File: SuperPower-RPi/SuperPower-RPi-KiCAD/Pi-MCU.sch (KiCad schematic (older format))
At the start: 39 parts, among them J10 Conn_01x04, J11 QWIIC_Connector, J12 DNP, J5 Conn_01x06, J7 Conn_01x03, J8 Conn_02x05_Odd_Even, J9 Conn_01x02, SW1 Tact, U3 STM32F412RETx, U4 ATtiny85-20SU, U5 ME6210A33M3G

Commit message: Chose component for Zener Diode and imported into PCB.
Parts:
- removed D6: D_Small, Diode_SMD:D_SOD-523, symbol Device:D_Small
- added D6: BZT585B13T-7, Diode_SMD:D_SOD-523, symbol Device:D_Zener_Small
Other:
- note added: "DotStar indicator"
- note added: "Extra I2C buss conn."
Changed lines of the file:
@@
-$EndComp
-$Comp
-L Device:D_Small D6
-U 1 1 5FAB9400
-P 6200 9650
-F 0 "D6" V 6246 9580 50  0000 R CNN
-F 1 "D_Small" V 6155 9580 50  0000 R CNN
-F 2 "Diode_SMD:D_SOD-523" V 6200 9650 50  0001 C CNN
-F 3 "~" V 6200 9650 50  0001 C CNN
-F 4 "FIX FOOTPRINT" H 6200 9650 50  0001 C CNN "Mfg"
-	1    6200 9650
-	0    -1   -1   0
 $EndComp
 $Comp
@@
 	1    0    0    -1
 $EndComp
+$Comp
+L Device:D_Zener_Small D?
+U 1 1 5FCDC76C
+P 6200 9650
+AR Path="/5F6AC66E/5FCDC76C" Ref="D?"  Part="1"
+AR Path="/5F6AC872/5FCDC76C" Ref="D6"  Part="1"
+F 0 "D6" V 6154 9720 50  0000 L CNN
+F 1 "BZT585B13T-7" V 6245 9720 50  0000 L CNN
+F 2 "Diode_SMD:D_SOD-523" V 6200 9650 50  0001 C CNN
+F 3 "https://www.diodes.com/assets/Datasheets/BZT585BxVxT.pdf" V 6200 9650 50  0001 C CNN
+F 4 "Diodes Incorporated" H 6200 9650 50  0001 C CNN "Mfg"
+F 5 "BZT585B13T-7" H 6200 9650 50  0001 C CNN "Mfg PN"
+F 6 "BZT585B13T-7DICT-ND" H 6200 9650 50  0001 C CNN "Digi-Key PN"
+	1    6200 9650
+	0    -1   -1   0
+$EndComp
+Text Notes 3500 10800 0    50   ~ 0
+Extra I2C buss conn.
+Text Notes 7950 10850 0    50   ~ 0
+DotStar indicator
 $EndSCHEMATC

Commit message: Updated meta-data.
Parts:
- C25, D8, JP1, JP4, JP5, JP6, R15, R25, R26, R27: Mfg (none) -> DNP
- C30: footprint Capacitor_SMD:C_0603_1608Metric -> Capacitor_SMD:C_0402_1005Metric
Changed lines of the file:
@@
 Text Label 2200 9600 2    50   ~ 0
 UART_TX
+Text Notes 3500 10800 0    50   ~ 0
+Extra I2C buss conn.
+Text Notes 7950 10850 0    50   ~ 0
+DotStar indicator
 $Comp
 L Device:R_Small R14
@@
 F 2 "Capacitor_SMD:C_0603_1608Metric" H 12000 5650 50  0001 C CNN
 F 3 "~" H 12000 5650 50  0001 C CNN
+F 4 "DNP" H 12000 5650 50  0001 C CNN "Mfg"
 	1    12000 5650
 	0    -1   1    0
@@
 F 0 "C30" H 5308 5104 50  0000 R CNN
 F 1 "10nF" H 5308 5195 50  0000 R CNN
-F 2 "Capacitor_SMD:C_0603_1608Metric" H 5400 5150 50  0001 C CNN
+F 2 "Capacitor_SMD:C_0402_1005Metric" H 5400 5150 50  0001 C CNN
 F 3 "~" H 5400 5150 50  0001 C CNN
 	1    5400 5150
@@
 F 2 "Resistor_SMD:R_0603_1608Metric" H 3250 10100 50  0001 C CNN
 F 3 "~" H 3250 10100 50  0001 C CNN
+F 4 "DNP" H 3250 10100 50  0001 C CNN "Mfg"
 	1    3250 10100
 	1    0    0    -1
@@
 F 2 "Resistor_SMD:R_0603_1608Metric" H 3550 10100 50  0001 C CNN
 F 3 "~" H 3550 10100 50  0001 C CNN
+F 4 "DNP" H 3550 10100 50  0001 C CNN "Mfg"
 	1    3550 10100
 	1    0    0    -1
@@
 F 2 "Jumper:SolderJumper-2_P1.3mm_Bridged_Pad1.0x1.5mm" H 5200 5800 50  0001 C CNN
 F 3 "~" H 5200 5800 50  0001 C CNN
+F 4 "DNP" H 5200 5800 50  0001 C CNN "Mfg"
 	1    5200 5800
 	1    0    0    -1
@@
 F 2 "LED_SMD:LED_0603_1608Metric" H 14650 6400 50  0001 C CNN
 F 3 "~" H 14650 6400 50  0001 C CNN
+F 4 "DNP" H 14650 6400 50  0001 C CNN "Mfg"
 	1    14650 6400
 	0    -1   -1   0
@@
 F 2 "Resistor_SMD:R_0603_1608Metric" H 14650 6100 50  0001 C CNN
 F 3 "~" H 14650 6100 50  0001 C CNN
+F 4 "DNP" H 14650 6100 50  0001 C CNN "Mfg"
 	1    14650 6100
 	1    0    0    1
@@
 F 2 "Resistor_SMD:R_0603_1608Metric" H 13150 6500 50  0001 C CNN
 F 3 "~" H 13150 6500 50  0001 C CNN
+F 4 "DNP" H 13150 6500 50  0001 C CNN "Mfg"
 	1    13150 6500
 	1    0    0    -1
@@
 F 2 "SuperPower-RPi-KiCAD:PinHeader_1x02_P2.54mm_Vertical_Shorted" H 3450 4250 50  0001 C CNN
 F 3 "~" H 3450 4250 50  0001 C CNN
+F 4 "DNP" H 3450 4250 50  0001 C CNN "Mfg"
 	1    3450 4250
 	1    0    0    -1
@@
 F 2 "Jumper:SolderJumper-2_P1.3mm_Open_Pad1.0x1.5mm" H 2500 5900 50  0001 C CNN
 F 3 "~" H 2500 5900 50  0001 C CNN
+F 4 "DNP" H 2500 5900 50  0001 C CNN "Mfg"
 	1    2500 5900
 	1    0    0    -1
@@
 F 2 "Jumper:SolderJumper-2_P1.3mm_Open_Pad1.0x1.5mm" H 9650 900 50  0001 C CNN
 F 3 "~" H 9650 900 50  0001 C CNN
+F 4 "DNP" H 9650 900 50  0001 C CNN "Mfg"
 	1    9650 900
 	1    0    0    -1
@@
 	0    -1   -1   0
 $EndComp
-Text Notes 3500 10800 0    50   ~ 0
-Extra I2C buss conn.
-Text Notes 7950 10850 0    50   ~ 0
-DotStar indicator
 $EndSCHEMATC

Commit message: Updated 1uF caps to 0402 package.
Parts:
- C32: footprint Capacitor_SMD:C_0603_1608Metric -> Capacitor_SMD:C_0402_1005Metric; Digi-Key PN (none) -> 490-10017-1-ND; Mfg (none) -> Murata Electronics; Mfg PN (none) -> GRM155R61E105KA12D
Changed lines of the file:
@@
 F 0 "C32" H 5708 5104 50  0000 R CNN
 F 1 "1.0uF" H 5708 5195 50  0000 R CNN
-F 2 "Capacitor_SMD:C_0603_1608Metric" H 5800 5150 50  0001 C CNN
+F 2 "Capacitor_SMD:C_0402_1005Metric" H 5800 5150 50  0001 C CNN
 F 3 "~" H 5800 5150 50  0001 C CNN
+F 4 "490-10017-1-ND" H 5800 5150 50  0001 C CNN "Digi-Key PN"
+F 5 "Murata Electronics" H 5800 5150 50  0001 C CNN "Mfg"
+F 6 "GRM155R61E105KA12D" H 5800 5150 50  0001 C CNN "Mfg PN"
 	1    5800 5150
 	-1   0    0    -1

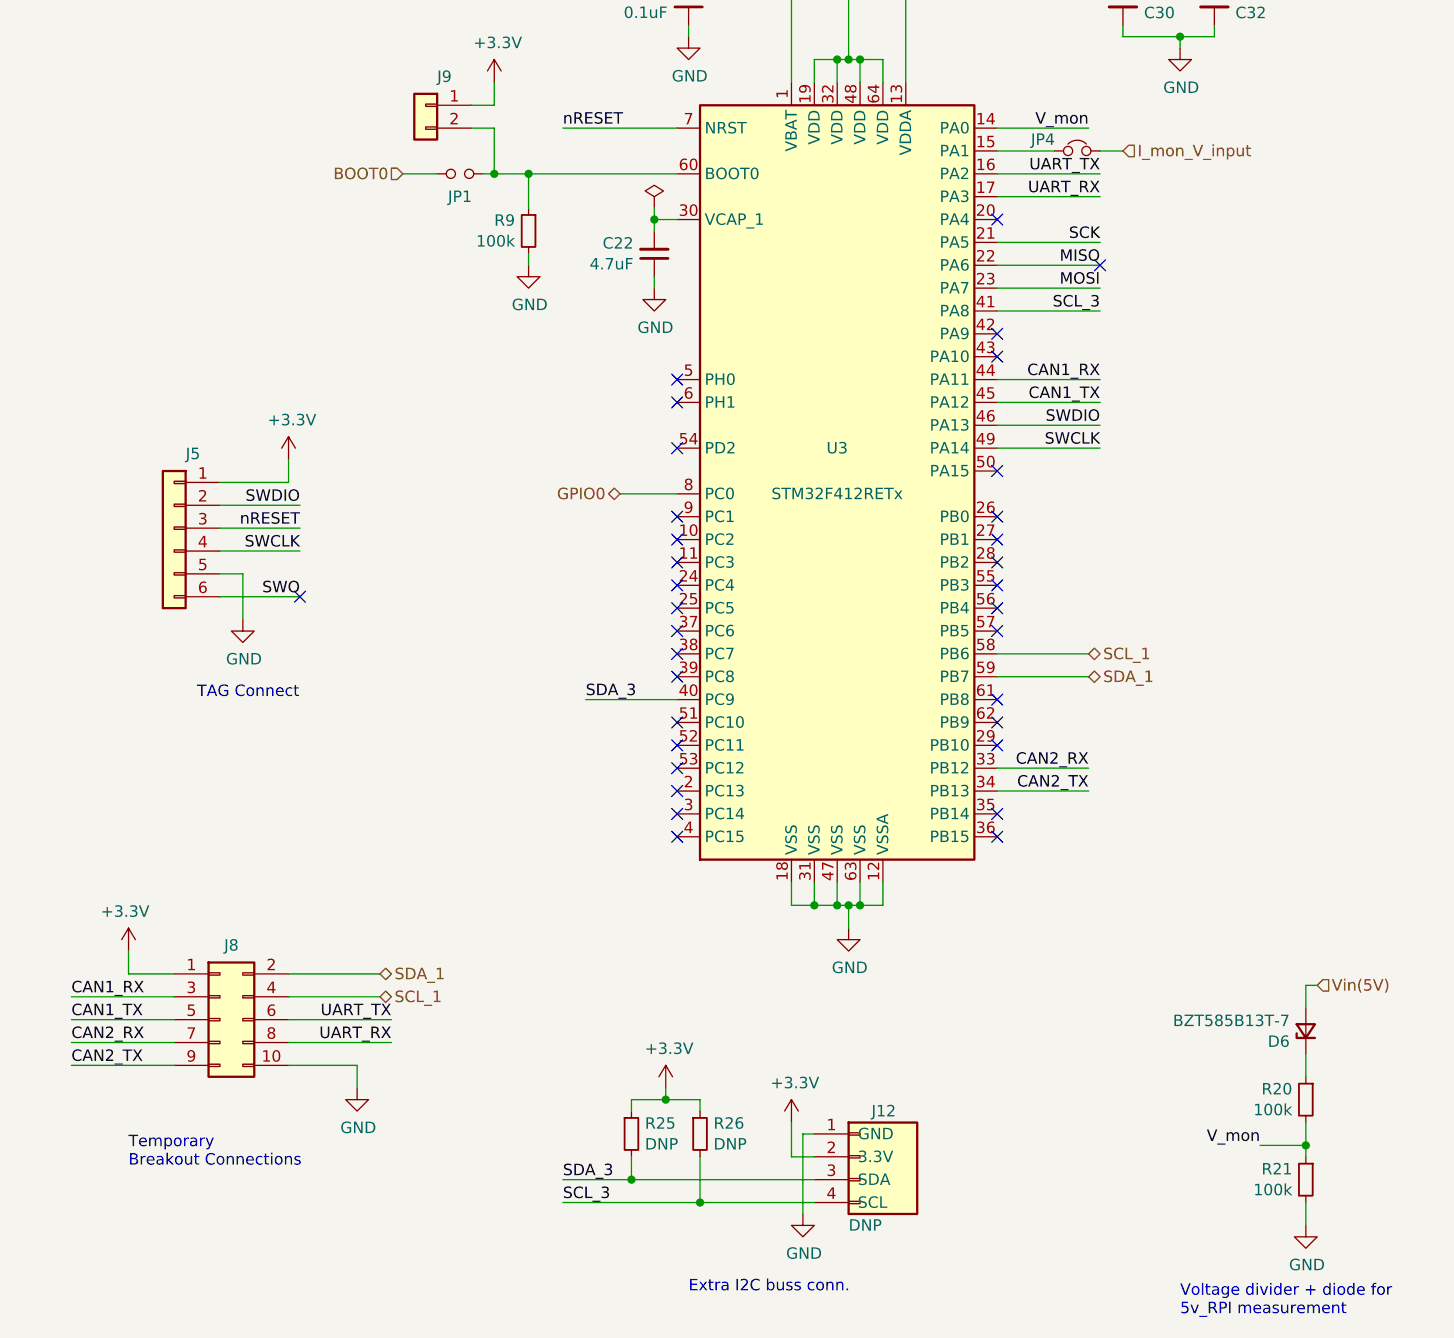
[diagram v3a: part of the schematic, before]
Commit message: Added Jumper to PC13 for bootloader switch.
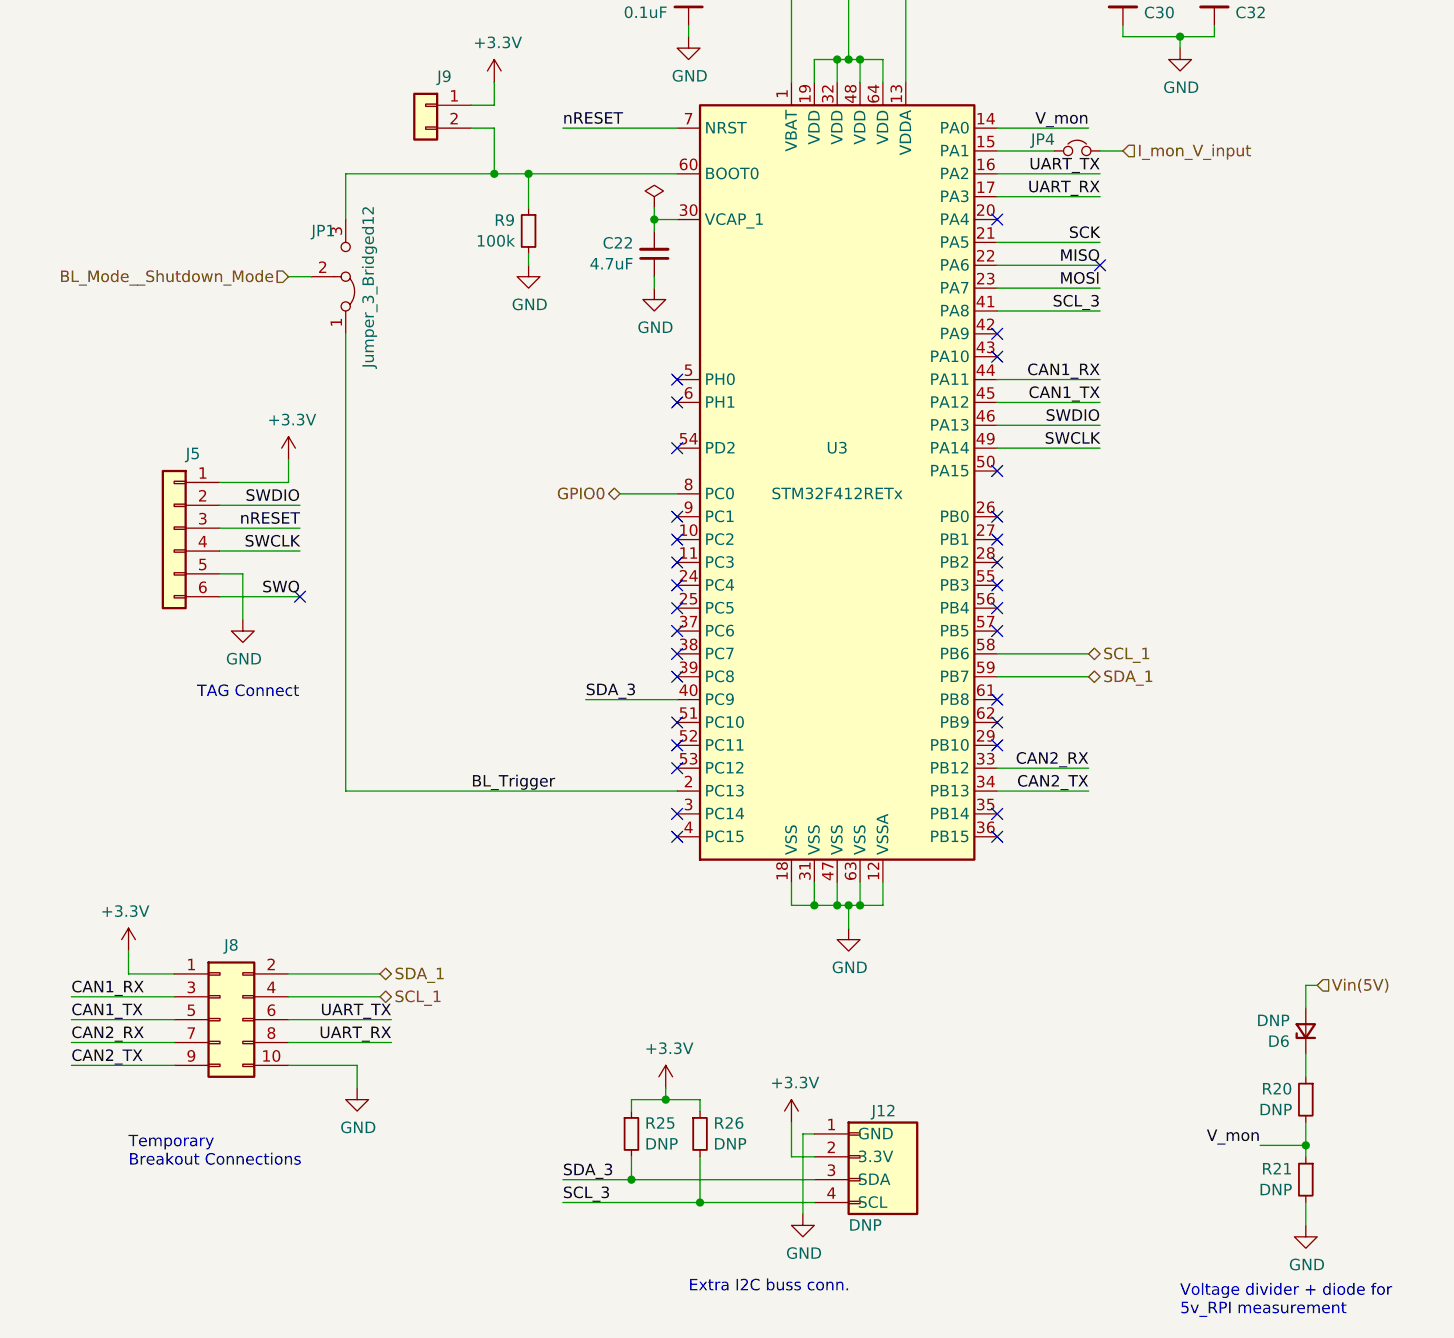
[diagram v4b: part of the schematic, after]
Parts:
- removed JP1: Jumper_NO_Small, Jumper:SolderJumper-2_P1.3mm_Open_Pad1.0x1.5mm, symbol Device:Jumper_NO_Small
- added JP1: Jumper_3_Bridged12, Jumper:SolderJumper-3_P1.3mm_Bridged12_RoundedPad1.0x1.5mm_NumberLabels, symbol Jumper:Jumper_3_Bridged12
- D6: value BZT585B13T-7 -> DNP
- R20, R21: value 100k -> DNP; footprint Resistor_SMD:R_0402_1005Metric -> Resistor_SMD:R_0603_1608Metric
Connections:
- net at J9.2 (Pin_2), R9.1, U3.60 (BOOT0): now also JP1.3 (B)
- net BL_Trigger: now reaches U3.2 (PC13)
- net BL_Trigger: now also JP1.1 (A)
- new net BL_Mode__Shutdown_Mode: JP1.2 (C)
- no-connect marks 35 -> 34
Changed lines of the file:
@@
 NoConn ~ 4850 7800
 NoConn ~ 4850 7900
-NoConn ~ 4850 8200
 NoConn ~ 4850 8300
 NoConn ~ 4850 8400
@@
 NoConn ~ 3450 8800
 NoConn ~ 3450 8700
-NoConn ~ 3450 8600
 NoConn ~ 3450 8500
 NoConn ~ 3450 8400
@@
 Text Notes 5650 10900 0    50   ~ 0
 Voltage divider + diode for\n5v_RPI measurement
-Text HLabel 2250 5900 0    50   Input ~ 0
-BOOT0
-Wire Wire Line
-	2600 5900 2650 5900
 Wire Wire Line
 	2550 5700 2650 5700
@@
 Wire Wire Line
 	2650 5900 2800 5900
-Wire Wire Line
-	2400 5900 2250 5900
 $Comp
 L power:+3.3V #PWR036
@@
 P 6200 10300
 F 0 "R21" H 6259 10346 50  0000 L CNN
-F 1 "100k" H 6259 10255 50  0000 L CNN
-F 2 "Resistor_SMD:R_0402_1005Metric" H 6200 10300 50  0001 C CNN
+F 1 "DNP" H 6259 10255 50  0000 L CNN
+F 2 "Resistor_SMD:R_0603_1608Metric" H 6200 10300 50  0001 C CNN
 F 3 "~" H 6200 10300 50  0001 C CNN
 	1    6200 10300
@@
 P 6200 9950
 F 0 "R20" H 6259 9996 50  0000 L CNN
-F 1 "100k" H 6259 9905 50  0000 L CNN
-F 2 "Resistor_SMD:R_0402_1005Metric" H 6200 9950 50  0001 C CNN
+F 1 "DNP" H 6259 9905 50  0000 L CNN
+F 2 "Resistor_SMD:R_0603_1608Metric" H 6200 9950 50  0001 C CNN
 F 3 "~" H 6200 9950 50  0001 C CNN
 	1    6200 9950
@@
 $EndComp
 $Comp
-L Device:Jumper_NO_Small JP1
-U 1 1 5FAAD012
-P 2500 5900
-F 0 "JP1" H 2500 5800 50  0000 C CNN
-F 1 "Jumper_NO_Small" H 2500 5994 50  0001 C CNN
-F 2 "Jumper:SolderJumper-2_P1.3mm_Open_Pad1.0x1.5mm" H 2500 5900 50  0001 C CNN
-F 3 "~" H 2500 5900 50  0001 C CNN
-F 4 "DNP" H 2500 5900 50  0001 C CNN "Mfg"
-	1    2500 5900
-	1    0    0    -1
-$EndComp
-$Comp
 L Connector_Generic:Conn_02x05_Odd_Even J8
 U 1 1 5FC8BD2A
@@
 AR Path="/5F6AC872/5FCDC76C" Ref="D6"  Part="1"
 F 0 "D6" V 6154 9720 50  0000 L CNN
-F 1 "BZT585B13T-7" V 6245 9720 50  0000 L CNN
+F 1 "DNP" V 6245 9720 50  0000 L CNN
 F 2 "Diode_SMD:D_SOD-523" V 6200 9650 50  0001 C CNN
 F 3 "https://www.diodes.com/assets/Datasheets/BZT585BxVxT.pdf" V 6200 9650 50  0001 C CNN
@@
 	0    -1   -1   0
 $EndComp
+NoConn ~ 4850 8200
+Text Label 2550 8600 0    50   ~ 0
+BL_Trigger
+Wire Wire Line
+	2000 8600 3450 8600
+Wire Wire Line
+	2000 5900 2650 5900
+$Comp
+L Jumper:Jumper_3_Bridged12 JP1
+U 1 1 5FD3DAEE
+P 2000 6350
+F 0 "JP1" V 2200 6200 50  0000 L CNN
+F 1 "Jumper_3_Bridged12" H 1600 6450 50  0000 L CNN
+F 2 "Jumper:SolderJumper-3_P1.3mm_Bridged12_RoundedPad1.0x1.5mm_NumberLabels" H 2000 6350 50  0001 C CNN
+F 3 "~" H 2000 6350 50  0001 C CNN
+	1    2000 6350
+	0    1    -1   0
+$EndComp
+Wire Wire Line
+	2000 8600 2000 6600
+Wire Wire Line
+	1850 6350 1750 6350
+Wire Wire Line
+	2000 6100 2000 5900
+Text HLabel 1750 6350 0    50   Input ~ 0
+BL_Mode__Shutdown_Mode
 $EndSCHEMATC

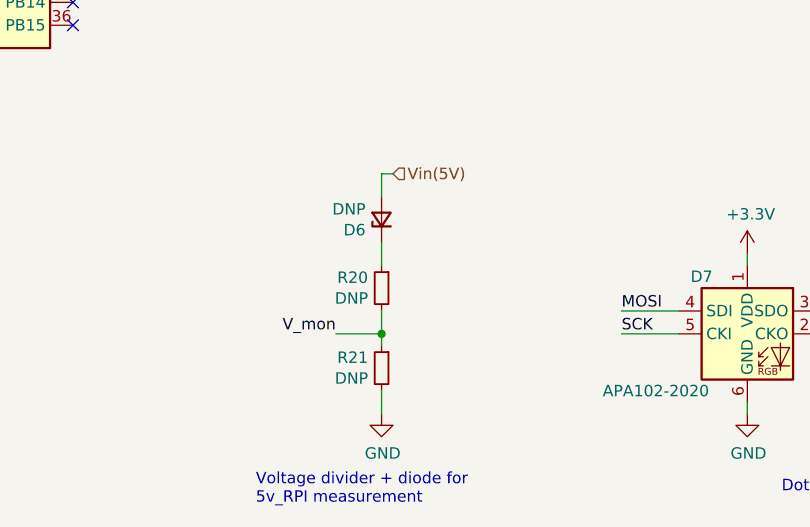
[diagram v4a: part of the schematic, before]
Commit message: Removed 5V measurement voltage divider.
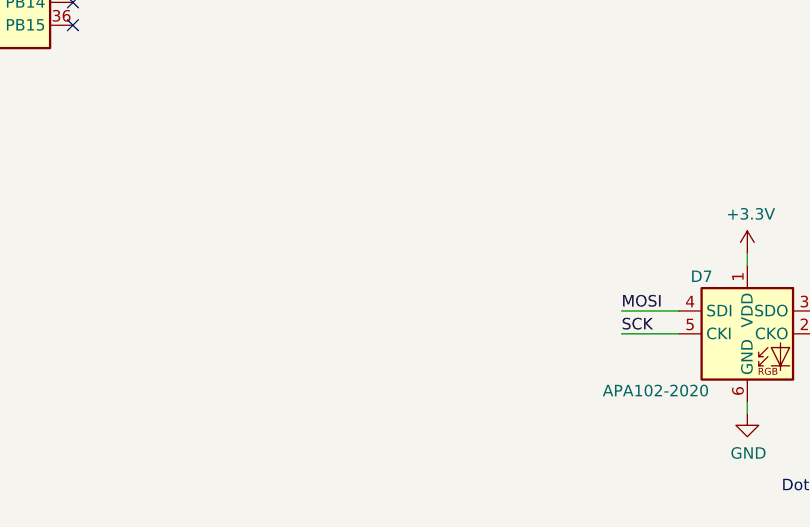
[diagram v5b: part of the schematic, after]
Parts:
- removed D6: DNP, Diode_SMD:D_SOD-523, symbol Device:D_Zener_Small
- removed R20, R21: DNP, Resistor_SMD:R_0603_1608Metric, symbol Device:R_Small
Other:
- note removed: "Voltage divider + diode for\n5v_RPI measurement"
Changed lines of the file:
@@
 	12650 6150 12300 6150
 NoConn ~ 12300 6550
-Text Notes 5650 10900 0    50   ~ 0
-Voltage divider + diode for\n5v_RPI measurement
 Wire Wire Line
 	2550 5700 2650 5700
@@
 $EndComp
 Connection ~ 2150 1150
-$Comp
-L power:GND #PWR038
-U 1 1 5FAAC254
-P 6200 10500
-F 0 "#PWR038" H 6200 10250 50  0001 C CNN
-F 1 "GND" H 6205 10327 50  0000 C CNN
-F 2 "" H 6200 10500 50  0001 C CNN
-F 3 "" H 6200 10500 50  0001 C CNN
-	1    6200 10500
-	1    0    0    -1
-$EndComp
-Wire Wire Line
-	6200 10500 6200 10400
-Wire Wire Line
-	6200 10200 6200 10150
-Wire Wire Line
-	6200 9850 6200 9750
-Text HLabel 6250 9450 2    50   Input ~ 0
-Vin(5V)
-Wire Wire Line
-	6200 9550 6200 9450
-Wire Wire Line
-	6200 9450 6250 9450
-Text Label 6000 10150 2    50   ~ 0
-V_mon
-Wire Wire Line
-	6000 10150 6200 10150
-Connection ~ 6200 10150
-Wire Wire Line
-	6200 10150 6200 10050
 Text Label 5250 5700 2    50   ~ 0
 V_mon
@@
 $EndComp
 $Comp
-L Device:R_Small R21
-U 1 1 5FAAB54D
-P 6200 10300
-F 0 "R21" H 6259 10346 50  0000 L CNN
-F 1 "DNP" H 6259 10255 50  0000 L CNN
-F 2 "Resistor_SMD:R_0603_1608Metric" H 6200 10300 50  0001 C CNN
-F 3 "~" H 6200 10300 50  0001 C CNN
-	1    6200 10300
-	-1   0    0    -1
-$EndComp
-$Comp
-L Device:R_Small R20
-U 1 1 5FAAC000
-P 6200 9950
-F 0 "R20" H 6259 9996 50  0000 L CNN
-F 1 "DNP" H 6259 9905 50  0000 L CNN
-F 2 "Resistor_SMD:R_0603_1608Metric" H 6200 9950 50  0001 C CNN
-F 3 "~" H 6200 9950 50  0001 C CNN
-	1    6200 9950
-	-1   0    0    -1
-$EndComp
-$Comp
 L MCU_Microchip_ATtiny:ATtiny85-20SU U4
 U 1 1 5FAE2AC9
@@
 	1    0    0    -1
 $EndComp
-$Comp
-L Device:D_Zener_Small D?
-U 1 1 5FCDC76C
-P 6200 9650
-AR Path="/5F6AC66E/5FCDC76C" Ref="D?"  Part="1"
-AR Path="/5F6AC872/5FCDC76C" Ref="D6"  Part="1"
-F 0 "D6" V 6154 9720 50  0000 L CNN
-F 1 "DNP" V 6245 9720 50  0000 L CNN
-F 2 "Diode_SMD:D_SOD-523" V 6200 9650 50  0001 C CNN
-F 3 "https://www.diodes.com/assets/Datasheets/BZT585BxVxT.pdf" V 6200 9650 50  0001 C CNN
-F 4 "Diodes Incorporated" H 6200 9650 50  0001 C CNN "Mfg"
-F 5 "BZT585B13T-7" H 6200 9650 50  0001 C CNN "Mfg PN"
-F 6 "BZT585B13T-7DICT-ND" H 6200 9650 50  0001 C CNN "Digi-Key PN"
-	1    6200 9650
-	0    -1   -1   0
-$EndComp
 NoConn ~ 4850 8200
